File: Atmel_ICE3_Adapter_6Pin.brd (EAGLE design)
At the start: 17.4 x 19.5 mm, 2 parts

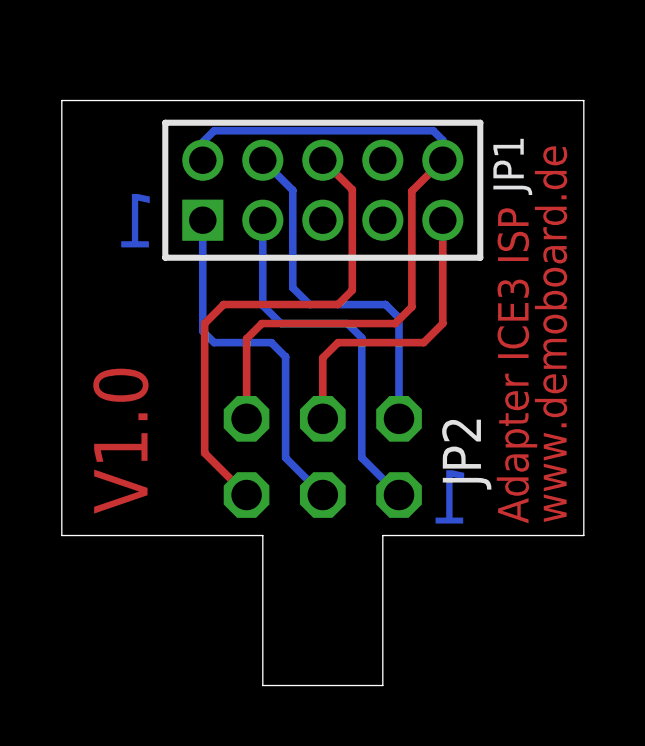
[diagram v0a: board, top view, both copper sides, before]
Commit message: Fix 6 pin wrong ICE3 header
Add 10 pin
Add gerber files
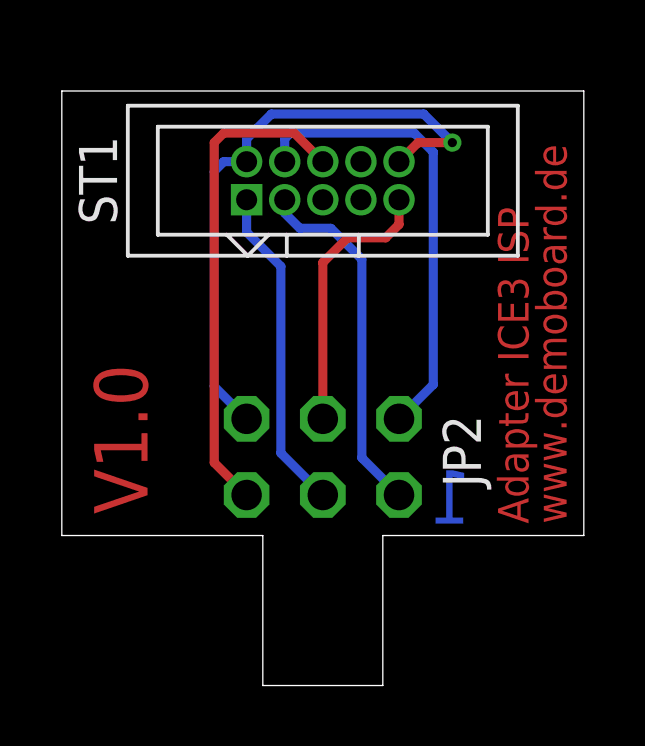
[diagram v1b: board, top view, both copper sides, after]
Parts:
- removed JP1: (no value), pinhead_2:2X05M
- added ST1: MA05-2_WANNE, pin-header-1.27:MA05-2_WANNE
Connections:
- net !SRST: now also ST1.6; no longer JP1.6
- net !TRST: now also ST1.8; no longer JP1.8
- net GND: now also ST1.10, ST1.2; no longer JP1.10, JP1.2
- net TCK: now also ST1.1; no longer JP1.1
- net TDI: now also ST1.9; no longer JP1.9
- net TDO: now also ST1.3; no longer JP1.3
- net TMS: now also ST1.5; no longer JP1.5
- net VTG: now also ST1.4; no longer JP1.4
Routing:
- net VTG: track 12.0 -> 15.4 mm
- net GND: track 23.5 -> 20.3 mm, vias 0 -> 1
- net TCK: track 11.9 -> 10.9 mm
- net TDI: track 9.95 -> 9.10 mm
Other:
- board size 17.4 x 19.5 mm -> 17.4 x 19.8 mm
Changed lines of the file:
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@@
 <wire x1="10.7" y1="0" x2="10.7" y2="5" width="0" layer="20"/>
 <wire x1="10.7" y1="5" x2="17.4" y2="5" width="0" layer="20"/>
-<wire x1="17.4" y1="5" x2="17.4" y2="19.5" width="0" layer="20"/>
-<wire x1="17.4" y1="19.5" x2="0" y2="19.5" width="0" layer="20"/>
-<wire x1="0" y1="19.5" x2="0" y2="5" width="0" layer="20"/>
+<wire x1="17.4" y1="5" x2="17.4" y2="19.8175" width="0" layer="20"/>
+<wire x1="17.4" y1="19.8175" x2="0" y2="19.8175" width="0" layer="20"/>
+<wire x1="0" y1="19.8175" x2="0" y2="5" width="0" layer="20"/>
 <wire x1="0" y1="5" x2="6.7" y2="5" width="0" layer="20"/>
 <wire x1="6.7" y1="5" x2="6.7" y2="0" width="0" layer="20"/>
@@
 <text x="2.8575" y="5.715" size="1.778" layer="1" font="vector" ratio="12" rot="R90">V1.0</text>
 <text x="13.6525" y="5.3975" size="1.778" layer="16" font="vector" ratio="12" rot="MR0">1</text>
-<text x="3.175" y="14.605" size="1.778" layer="16" font="vector" ratio="12" rot="MR0">1</text>
 </plain>
 <attributes>
@@
 </autorouter>
 <elements>
-<element name="JP1" library="pinhead_2" package="2X05M" value="" x="8.7" y="16.51" smashed="yes">
-<attribute name="NAME" x="15.4" y="16.415" size="1.016" layer="25" ratio="14" rot="R90"/>
-<attribute name="VALUE" x="15.7" y="14.51" size="0.8128" layer="27" ratio="10" rot="R90"/>
-</element>
 <element name="JP2" library="pinhead_2" package="2X03" value="" x="8.7" y="7.62" smashed="yes" rot="MR0">
 <attribute name="NAME" x="12.7" y="9.0175" size="1.27" layer="25" ratio="10" rot="R270"/>
 <attribute name="VALUE" x="12.51" y="3.175" size="1.27" layer="28" rot="MR0"/>
 </element>
+<element name="ST1" library="pin-header-1.27" package="MA05-2_WANNE" value="MA05-2_WANNE" x="8.7" y="16.8275" smashed="yes">
+<attribute name="NAME" x="1.8415" y="15.3675" size="1.27" layer="25" ratio="10" rot="R90"/>
+</element>
 </elements>
 <signals>
 <signal name="TCK">
-<contactref element="JP1" pad="1"/>
 <contactref element="JP2" pad="3"/>
-<wire x1="8.7" y1="6.35" x2="7.46125" y2="7.58875" width="0.254" layer="16"/>
-<wire x1="7.46125" y1="7.58875" x2="7.46125" y2="10.95375" width="0.254" layer="16"/>
-<wire x1="7.46125" y1="10.95375" x2="6.985" y2="11.43" width="0.254" layer="16"/>
-<wire x1="6.985" y1="11.43" x2="5.08" y2="11.43" width="0.254" layer="16"/>
-<wire x1="5.08" y1="11.43" x2="4.7" y2="11.81" width="0.254" layer="16"/>
-<wire x1="4.7" y1="11.81" x2="4.7" y2="15.51" width="0.254" layer="16"/>
+<contactref element="ST1" pad="1"/>
+<wire x1="6.16" y1="16.1925" x2="6.16" y2="15.1125" width="0.3048" layer="16"/>
+<wire x1="6.16" y1="15.1125" x2="7.3025" y2="13.97" width="0.3048" layer="16"/>
+<wire x1="7.3025" y1="13.97" x2="7.3025" y2="7.7475" width="0.3048" layer="16"/>
+<wire x1="7.3025" y1="7.7475" x2="8.7" y2="6.35" width="0.3048" layer="16"/>
 </signal>
 <signal name="TDO">
-<contactref element="JP1" pad="3"/>
 <contactref element="JP2" pad="1"/>
-<wire x1="11.24" y1="6.35" x2="10.00125" y2="7.58875" width="0.254" layer="16"/>
-<wire x1="10.00125" y1="7.58875" x2="10.00125" y2="11.58875" width="0.254" layer="16"/>
-<wire x1="10.00125" y1="11.58875" x2="9.525" y2="12.065" width="0.254" layer="16"/>
-<wire x1="9.525" y1="12.065" x2="7.3025" y2="12.065" width="0.254" layer="16"/>
-<wire x1="7.3025" y1="12.065" x2="6.7" y2="12.6675" width="0.254" layer="16"/>
-<wire x1="6.7" y1="12.6675" x2="6.7" y2="15.51" width="0.254" layer="16"/>
+<contactref element="ST1" pad="3"/>
+<wire x1="7.43" y1="16.1925" x2="7.43" y2="15.7475" width="0.3048" layer="16"/>
+<wire x1="7.43" y1="15.7475" x2="7.9375" y2="15.24" width="0.3048" layer="16"/>
+<wire x1="7.9375" y1="15.24" x2="8.969375" y2="15.24" width="0.3048" layer="16"/>
+<wire x1="8.969375" y1="15.24" x2="10.00125" y2="14.208125" width="0.3048" layer="16"/>
+<wire x1="10.00125" y1="14.208125" x2="10.00125" y2="7.58875" width="0.3048" layer="16"/>
+<wire x1="10.00125" y1="7.58875" x2="11.24" y2="6.35" width="0.3048" layer="16"/>
+</signal>
+<signal name="TDI">
+<contactref element="JP2" pad="4"/>
+<contactref element="ST1" pad="9"/>
+<wire x1="11.24" y1="16.1925" x2="11.24" y2="15.3675" width="0.3048" layer="1"/>
+<wire x1="11.24" y1="15.3675" x2="10.795" y2="14.9225" width="0.3048" layer="1"/>
+<wire x1="10.795" y1="14.9225" x2="9.525" y2="14.9225" width="0.3048" layer="1"/>
+<wire x1="9.525" y1="14.9225" x2="8.7" y2="14.0975" width="0.3048" layer="1"/>
+<wire x1="8.7" y1="14.0975" x2="8.7" y2="8.89" width="0.3048" layer="1"/>
+</signal>
+<signal name="GND">
+<contactref element="JP2" pad="6"/>
+<contactref element="ST1" pad="2"/>
+<contactref element="ST1" pad="10"/>
+<wire x1="6.16" y1="17.4625" x2="5.3975" y2="17.4625" width="0.3048" layer="16"/>
+<wire x1="5.3975" y1="17.4625" x2="5.08" y2="17.145" width="0.3048" layer="16"/>
+<wire x1="5.08" y1="17.145" x2="5.08" y2="9.97" width="0.3048" layer="16"/>
+<wire x1="5.08" y1="9.97" x2="6.16" y2="8.89" width="0.3048" layer="16"/>
+<wire x1="6.16" y1="17.4625" x2="6.16" y2="18.225" width="0.3048" layer="16"/>
+<wire x1="6.16" y1="18.225" x2="6.985" y2="19.05" width="0.3048" layer="16"/>
+<wire x1="6.985" y1="19.05" x2="12.065" y2="19.05" width="0.3048" layer="16"/>
+<wire x1="12.065" y1="19.05" x2="13.0175" y2="18.0975" width="0.3048" layer="16"/>
+<via x="13.0175" y="18.0975" extent="1-16" drill="0.3048"/>
+<wire x1="13.0175" y1="18.0975" x2="11.875" y2="18.0975" width="0.3048" layer="1"/>
+<wire x1="11.875" y1="18.0975" x2="11.24" y2="17.4625" width="0.3048" layer="1"/>
+</signal>
+<signal name="VTG">
+<contactref element="JP2" pad="2"/>
+<contactref element="ST1" pad="4"/>
+<wire x1="7.43" y1="17.4625" x2="7.43" y2="18.225" width="0.3048" layer="16"/>
+<wire x1="7.43" y1="18.225" x2="7.62" y2="18.415" width="0.3048" layer="16"/>
+<wire x1="7.62" y1="18.415" x2="11.7475" y2="18.415" width="0.3048" layer="16"/>
+<wire x1="11.7475" y1="18.415" x2="12.3825" y2="17.78" width="0.3048" layer="16"/>
+<wire x1="12.3825" y1="17.78" x2="12.3825" y2="10.0325" width="0.3048" layer="16"/>
+<wire x1="12.3825" y1="10.0325" x2="11.24" y2="8.89" width="0.3048" layer="16"/>
+</signal>
+<signal name="!SRST">
+<contactref element="JP2" pad="5"/>
+<contactref element="ST1" pad="6"/>
+<wire x1="8.7" y1="17.4625" x2="7.7475" y2="18.415" width="0.3048" layer="1"/>
+<wire x1="7.7475" y1="18.415" x2="5.3975" y2="18.415" width="0.3048" layer="1"/>
+<wire x1="5.3975" y1="18.415" x2="5.08" y2="18.0975" width="0.3048" layer="1"/>
+<wire x1="5.08" y1="18.0975" x2="5.08" y2="7.43" width="0.3048" layer="1"/>
+<wire x1="5.08" y1="7.43" x2="6.16" y2="6.35" width="0.3048" layer="1"/>
+</signal>
+<signal name="!TRST">
+<contactref element="ST1" pad="8"/>
 </signal>
 <signal name="TMS">
-<contactref element="JP1" pad="5"/>
-</signal>
-<signal name="TDI">
-<contactref element="JP1" pad="9"/>
-<contactref element="JP2" pad="4"/>
-<wire x1="8.7" y1="8.89" x2="8.7" y2="10.9225" width="0.254" layer="1"/>
-<wire x1="8.7" y1="10.9225" x2="9.2075" y2="11.43" width="0.254" layer="1"/>
-<wire x1="9.2075" y1="11.43" x2="12.065" y2="11.43" width="0.254" layer="1"/>
-<wire x1="12.065" y1="11.43" x2="12.7" y2="12.065" width="0.254" layer="1"/>
-<wire x1="12.7" y1="12.065" x2="12.7" y2="15.51" width="0.254" layer="1"/>
-</signal>
-<signal name="GND">
-<contactref element="JP1" pad="2"/>
-<contactref element="JP1" pad="10"/>
-<contactref element="JP2" pad="6"/>
-<wire x1="4.7" y1="17.51" x2="4.7" y2="18.114375" width="0.254" layer="16"/>
-<wire x1="4.7" y1="18.114375" x2="5.08" y2="18.494375" width="0.254" layer="16"/>
-<wire x1="5.08" y1="18.494375" x2="12.3825" y2="18.494375" width="0.254" layer="16"/>
-<wire x1="12.3825" y1="18.494375" x2="12.7" y2="18.176875" width="0.254" layer="16"/>
-<wire x1="12.7" y1="18.176875" x2="12.7" y2="17.51" width="0.254" layer="16"/>
-<wire x1="6.16" y1="8.89" x2="6.16" y2="11.5575" width="0.254" layer="1"/>
-<wire x1="6.16" y1="11.5575" x2="6.6675" y2="12.065" width="0.254" layer="1"/>
-<wire x1="6.6675" y1="12.065" x2="11.1125" y2="12.065" width="0.254" layer="1"/>
-<wire x1="11.668125" y1="12.620625" x2="11.668125" y2="16.478125" width="0.254" layer="1"/>
-<wire x1="11.668125" y1="16.478125" x2="12.7" y2="17.51" width="0.254" layer="1"/>
-<wire x1="11.1125" y1="12.065" x2="11.668125" y2="12.620625" width="0.254" layer="1"/>
-</signal>
-<signal name="VTG">
-<contactref element="JP1" pad="4"/>
-<contactref element="JP2" pad="2"/>
-<wire x1="11.24" y1="8.89" x2="11.24" y2="12.255" width="0.254" layer="16"/>
-<wire x1="11.24" y1="12.255" x2="10.795" y2="12.7" width="0.254" layer="16"/>
-<wire x1="10.795" y1="12.7" x2="8.255" y2="12.7" width="0.254" layer="16"/>
-<wire x1="8.255" y1="12.7" x2="7.699375" y2="13.255625" width="0.254" layer="16"/>
-<wire x1="7.699375" y1="13.255625" x2="7.699375" y2="16.510625" width="0.254" layer="16"/>
-<wire x1="7.699375" y1="16.510625" x2="6.7" y2="17.51" width="0.254" layer="16"/>
-</signal>
-<signal name="!SRST">
-<contactref element="JP1" pad="6"/>
-<contactref element="JP2" pad="5"/>
-<wire x1="6.16" y1="6.35" x2="4.7625" y2="7.7475" width="0.254" layer="1"/>
-<wire x1="4.7625" y1="7.7475" x2="4.7625" y2="12.065" width="0.254" layer="1"/>
-<wire x1="4.7625" y1="12.065" x2="5.3975" y2="12.7" width="0.254" layer="1"/>
-<wire x1="5.3975" y1="12.7" x2="9.2075" y2="12.7" width="0.254" layer="1"/>
-<wire x1="9.2075" y1="12.7" x2="9.68375" y2="13.17625" width="0.254" layer="1"/>
-<wire x1="9.68375" y1="13.17625" x2="9.68375" y2="16.52625" width="0.254" layer="1"/>
-<wire x1="9.68375" y1="16.52625" x2="8.7" y2="17.51" width="0.254" layer="1"/>
-</signal>
-<signal name="!TRST">
-<contactref element="JP1" pad="8"/>
+<contactref element="ST1" pad="5"/>
 </signal>
 </signals>
